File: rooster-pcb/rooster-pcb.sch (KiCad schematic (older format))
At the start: 95 parts, among them SW0-0 SW_Push, SW0-1 SW_Push, SW0-10 SW_Push, SW0-11 SW_Push, SW0-2 SW_Push, SW0-3 SW_Push, SW0-4 SW_Push, SW0-5 SW_Push, SW0-6 SW_Push, SW0-7 SW_Push, SW0-8 SW_Push, SW0-9 SW_Push, SW1-0 SW_Push, SW1-1 SW_Push, SW1-10 SW_Push, SW1-11 SW_Push, SW1-2 SW_Push, SW1-3 SW_Push, SW1-4 SW_Push, SW1-5 SW_Push, SW1-6 SW_Push, SW1-7 SW_Push, SW1-8 SW_Push, SW1-9 SW_Push, SW2-0 SW_Push, SW2-1 SW_Push, SW2-10 SW_Push, SW2-11 SW_Push, SW2-2 SW_Push, SW2-3 SW_Push, SW2-4 SW_Push, SW2-5 SW_Push, SW2-6 SW_Push, SW2-7 SW_Push, SW2-8 SW_Push, SW2-9 SW_Push, SW3-0 SW_Push, SW3-1 SW_Push, SW3-10 SW_Push, SW3-11 SW_Push, SW3-2 SW_Push, SW3-3 SW_Push, SW3-4 SW_Push, SW3-5 SW_Push, SW3-7 SW_Push, SW3-8 SW_Push, SW3-9 SW_Push, U1 Sparkfun_Pro_Micro

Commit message: Replaced ProMicro symbol & footprint; adding mounting holes
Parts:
- removed U1: Sparkfun_Pro_Micro, Arduino:Sparkfun_Pro_Micro, symbol Arduino:Sparkfun_Pro_Micro
- added U1: ProMicro, Keyboard_Components:ArduinoProMicro, symbol Keyboard_Components:ProMicro
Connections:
- net +5V: now also U1.21 (VCC)
- net COL0: now also U1.5 (2/PD1)
- net COL1: now also U1.6 (3/PD0)
- net COL2: now also U1.7 (4/PD4)
- net COL3: now also U1.8 (5/PC6)
- net COL4: now also U1.13 (10/PB6)
- net COL5: now also U1.14 (16/PB2)
- net COL6: now also U1.15 (14/PB3)
- net COL7: now also U1.16 (15/PB1)
- net COL8: now also U1.17 (A0/PF7)
- net COL9: now also U1.18 (A1/PF6)
- net GND: now also U1.23 (GND), U1.3 (GND), U1.4 (GND)
- net ROW0: now also U1.9 (6/PD7)
- net ROW1: now also U1.10 (7/PE6)
- net ROW2: now also U1.11 (8/PB4)
- net ROW3: now also U1.12 (9/PB5)
- net COLA renamed COL10
- net COL10: now also U1.19 (A2/PF5)
- net COLB renamed COL11
- net COL11: now also U1.20 (A3/PF4)
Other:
- note added: "Keyboard key matrix"
- note added: "Microcontroller board\n(SparkFun Pro Micro or compatible)"
- note removed: "Note: all switches and diodes are named by their row and column.\nFor instance, SW3-7 is the switch in row 3, column 7."
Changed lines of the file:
@@
 Comment4 ""
 $EndDescr
-$Comp
-L Arduino:Sparkfun_Pro_Micro U1
-U 1 1 6015F3D8
-P 1600 1700
-F 0 "U1" H 1600 2589 60  0000 C CNN
-F 1 "Sparkfun_Pro_Micro" H 1600 2483 60  0000 C CNN
-F 2 "Arduino:Sparkfun_Pro_Micro" H 1600 1050 60  0001 C CNN
-F 3 "https://www.sparkfun.com/products/12640" H 1700 650 60  0001 C CNN
-	1    1600 1700
-	1    0    0    -1
-$EndComp
-$Comp
-L power:GND #PWR0101
-U 1 1 6016D49B
-P 1000 1300
-F 0 "#PWR0101" H 1000 1050 50  0001 C CNN
-F 1 "GND" V 1005 1172 50  0000 R CNN
-F 2 "" H 1000 1300 50  0001 C CNN
-F 3 "" H 1000 1300 50  0001 C CNN
-	1    1000 1300
-	0    1    1    0
-$EndComp
-$Comp
-L power:GND #PWR0102
-U 1 1 6016ED65
-P 1000 1400
-F 0 "#PWR0102" H 1000 1150 50  0001 C CNN
-F 1 "GND" V 1005 1272 50  0000 R CNN
-F 2 "" H 1000 1400 50  0001 C CNN
-F 3 "" H 1000 1400 50  0001 C CNN
-	1    1000 1400
-	0    1    1    0
-$EndComp
-$Comp
-L power:GND #PWR0103
-U 1 1 60170089
-P 2200 1200
-F 0 "#PWR0103" H 2200 950 50  0001 C CNN
-F 1 "GND" V 2205 1072 50  0000 R CNN
-F 2 "" H 2200 1200 50  0001 C CNN
-F 3 "" H 2200 1200 50  0001 C CNN
-	1    2200 1200
-	0    -1   -1   0
-$EndComp
-$Comp
-L power:+5V #PWR0104
-U 1 1 601759BB
-P 2200 1400
-F 0 "#PWR0104" H 2200 1250 50  0001 C CNN
-F 1 "+5V" V 2215 1528 50  0000 L CNN
-F 2 "" H 2200 1400 50  0001 C CNN
-F 3 "" H 2200 1400 50  0001 C CNN
-	1    2200 1400
-	0    1    1    0
-$EndComp
-Text GLabel 1000 1200 0    50   Input ~ 0
-COL0
-Text GLabel 1000 1100 0    50   Input ~ 0
-COL1
-Text GLabel 1000 1500 0    50   Input ~ 0
-COL2
-Text GLabel 1000 1600 0    50   Input ~ 0
-COL3
-Text GLabel 1000 1700 0    50   Input ~ 0
-COL4
-Text GLabel 1000 1800 0    50   Input ~ 0
-COL5
-Text GLabel 1000 1900 0    50   Input ~ 0
-COL6
-Text GLabel 1000 2100 0    50   Input ~ 0
-COL8
-Text GLabel 1000 2000 0    50   Input ~ 0
-COL7
-Text GLabel 1000 2200 0    50   Input ~ 0
-COL9
-Text GLabel 2200 2200 2    50   Input ~ 0
-COLA
-Text GLabel 2200 2100 2    50   Input ~ 0
-COLB
-Text GLabel 2200 2000 2    50   Input ~ 0
-ROW0
-Text GLabel 2200 1900 2    50   Input ~ 0
-ROW1
-Text GLabel 2200 1800 2    50   Input ~ 0
-ROW2
 Text GLabel 3250 3000 0    50   Input ~ 0
 ROW1
@@
 ROW0
 Text GLabel 11050 1000 1    50   Input ~ 0
-COLB
+COL11
 Text GLabel 10400 1000 1    50   Input ~ 0
-COLA
+COL10
 Text GLabel 9750 1000 1    50   Input ~ 0
 COL9
@@
 Text GLabel 3250 5000 0    50   Input ~ 0
 ROW3
-Text GLabel 2200 1700 2    50   Input ~ 0
-ROW3
 $Comp
 L Switch:SW_Push SW3-0
@@
 Text Notes 7350 4600 0    39   ~ 0
 (No SW3-6 here\nbecause SW3-5 \nis the 2U-wide\nspace bar.)
-Text Notes 8000 5500 0    50   ~ 0
-Note: all switches and diodes are named by their row and column.\nFor instance, SW3-7 is the switch in row 3, column 7.
-NoConn ~ 2200 1100
-NoConn ~ 2200 1300
-NoConn ~ 2200 1500
-NoConn ~ 2200 1600
 $Comp
 L Diode:1N4148 D1-7
@@
 	0    -1   -1   0
 $EndComp
+$Comp
+L Keyboard_Components:ProMicro U1
+U 1 1 601921A6
+P 1750 1650
+F 0 "U1" H 1750 2487 60  0000 C CNN
+F 1 "ProMicro" H 1750 2381 60  0000 C CNN
+F 2 "Keyboard_Components:ArduinoProMicro" V 2800 -850 60  0001 C CNN
+F 3 "" V 2800 -850 60  0001 C CNN
+	1    1750 1650
+	1    0    0    -1
+$EndComp
+$Comp
+L power:+5V #PWR0101
+U 1 1 601A002E
+P 2450 1400
+F 0 "#PWR0101" H 2450 1250 50  0001 C CNN
+F 1 "+5V" V 2465 1528 50  0000 L CNN
+F 2 "" H 2450 1400 50  0001 C CNN
+F 3 "" H 2450 1400 50  0001 C CNN
+	1    2450 1400
+	0    1    1    0
+$EndComp
+$Comp
+L power:GND #PWR0102
+U 1 1 601A0D97
+P 2450 1200
+F 0 "#PWR0102" H 2450 950 50  0001 C CNN
+F 1 "GND" V 2455 1072 50  0000 R CNN
+F 2 "" H 2450 1200 50  0001 C CNN
+F 3 "" H 2450 1200 50  0001 C CNN
+	1    2450 1200
+	0    -1   -1   0
+$EndComp
+$Comp
+L power:GND #PWR0103
+U 1 1 601A1867
+P 1050 1300
+F 0 "#PWR0103" H 1050 1050 50  0001 C CNN
+F 1 "GND" V 1055 1172 50  0000 R CNN
+F 2 "" H 1050 1300 50  0001 C CNN
+F 3 "" H 1050 1300 50  0001 C CNN
+	1    1050 1300
+	0    1    1    0
+$EndComp
+$Comp
+L power:GND #PWR0104
+U 1 1 601A22AF
+P 1050 1400
+F 0 "#PWR0104" H 1050 1150 50  0001 C CNN
+F 1 "GND" V 1055 1272 50  0000 R CNN
+F 2 "" H 1050 1400 50  0001 C CNN
+F 3 "" H 1050 1400 50  0001 C CNN
+	1    1050 1400
+	0    1    1    0
+$EndComp
+Text GLabel 1050 1500 0    50   Input ~ 0
+COL0
+Text GLabel 1050 1600 0    50   Input ~ 0
+COL1
+Text GLabel 1050 1700 0    50   Input ~ 0
+COL2
+Text GLabel 1050 1800 0    50   Input ~ 0
+COL3
+Text GLabel 1050 1900 0    50   Input ~ 0
+ROW0
+Text GLabel 1050 2000 0    50   Input ~ 0
+ROW1
+Text GLabel 1050 2100 0    50   Input ~ 0
+ROW2
+Text GLabel 1050 2200 0    50   Input ~ 0
+ROW3
+Text GLabel 2450 1500 2    50   Input ~ 0
+COL11
+Text GLabel 2450 1600 2    50   Input ~ 0
+COL10
+Text GLabel 2450 1700 2    50   Input ~ 0
+COL9
+Text GLabel 2450 1800 2    50   Input ~ 0
+COL8
+Text GLabel 2450 1900 2    50   Input ~ 0
+COL7
+NoConn ~ 2450 1100
+NoConn ~ 2450 1300
+Text GLabel 2450 2000 2    50   Input ~ 0
+COL6
+Text GLabel 2450 2100 2    50   Input ~ 0
+COL5
+Text GLabel 2450 2200 2    50   Input ~ 0
+COL4
+NoConn ~ 1050 1100
+NoConn ~ 1050 1200
+Text Notes 800  2700 0    79   ~ 0
+Microcontroller board\n(SparkFun Pro Micro or compatible)
+Text Notes 3500 5350 0    79   ~ 0
+Keyboard key matrix
 $EndSCHEMATC

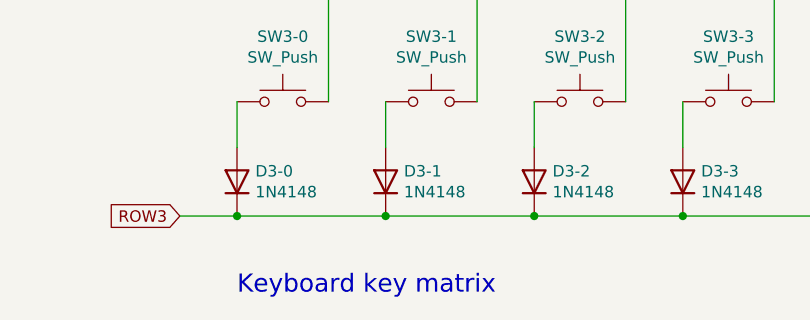
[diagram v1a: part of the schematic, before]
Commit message: Positioned diodes
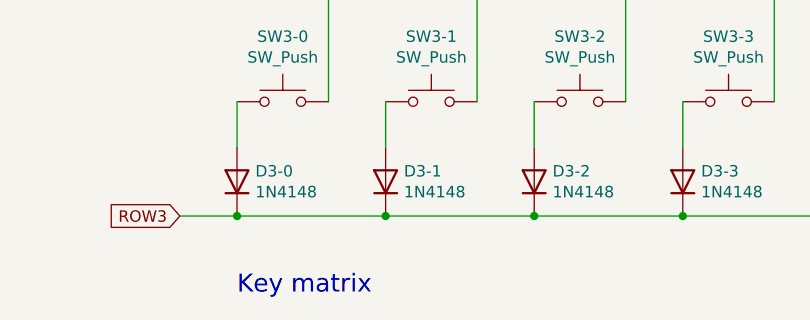
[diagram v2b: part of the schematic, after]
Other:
- note added: "Key matrix"
- note removed: "Keyboard key matrix"
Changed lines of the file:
@@
 Microcontroller board\n(SparkFun Pro Micro or compatible)
 Text Notes 3500 5350 0    79   ~ 0
-Keyboard key matrix
+Key matrix
 $EndSCHEMATC

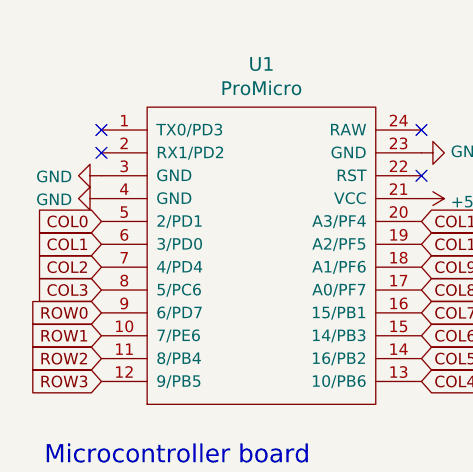
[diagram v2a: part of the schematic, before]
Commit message: Remade PCB for 0.5mm spacing between keycaps + surface-mounted diodes
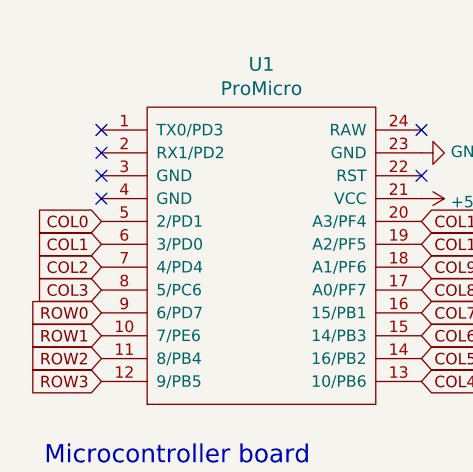
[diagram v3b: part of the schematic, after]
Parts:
- D0-0, D0-1, D0-10, D0-11, D0-2, D0-3, D0-4, D0-5, D0-6, D0-7, D0-8, D0-9, D1-0, D1-1, D1-10, D1-11, D1-2, D1-3, D1-4, D1-5, D1-6, D1-7, D1-8, D1-9, D2-0, D2-1, D2-10, D2-11, D2-2, D2-3, D2-4, D2-5, D2-6, D2-7, D2-8, D2-9, D3-0, D3-1, D3-10, D3-11, D3-2, D3-3, D3-4, D3-5, D3-7, D3-8, D3-9: footprint Diode_THT:D_DO-35_SOD27_P7.62mm_Horizontal -> Diode_SMD:D_SOD-123
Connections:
- net GND: no longer U1.3 (GND), U1.4 (GND)
- no-connect marks 4 -> 6
